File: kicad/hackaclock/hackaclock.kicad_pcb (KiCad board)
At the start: 2 copper layers, 95 x 65 mm, 13 parts, among them J1 Conn_01x08_Pin, SW1 SW_Push, SW2 SW_Push, SW3 SW_Push, SW4 SW_Push, SW5 SW_Push, SW6 SW_Push, U1 XIAO-ESP32-C3-SMD

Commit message: Added stardance logo to silkscreen
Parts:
- added G***: LOGO, LOGO, F.Cu at (41.0, 28.0)

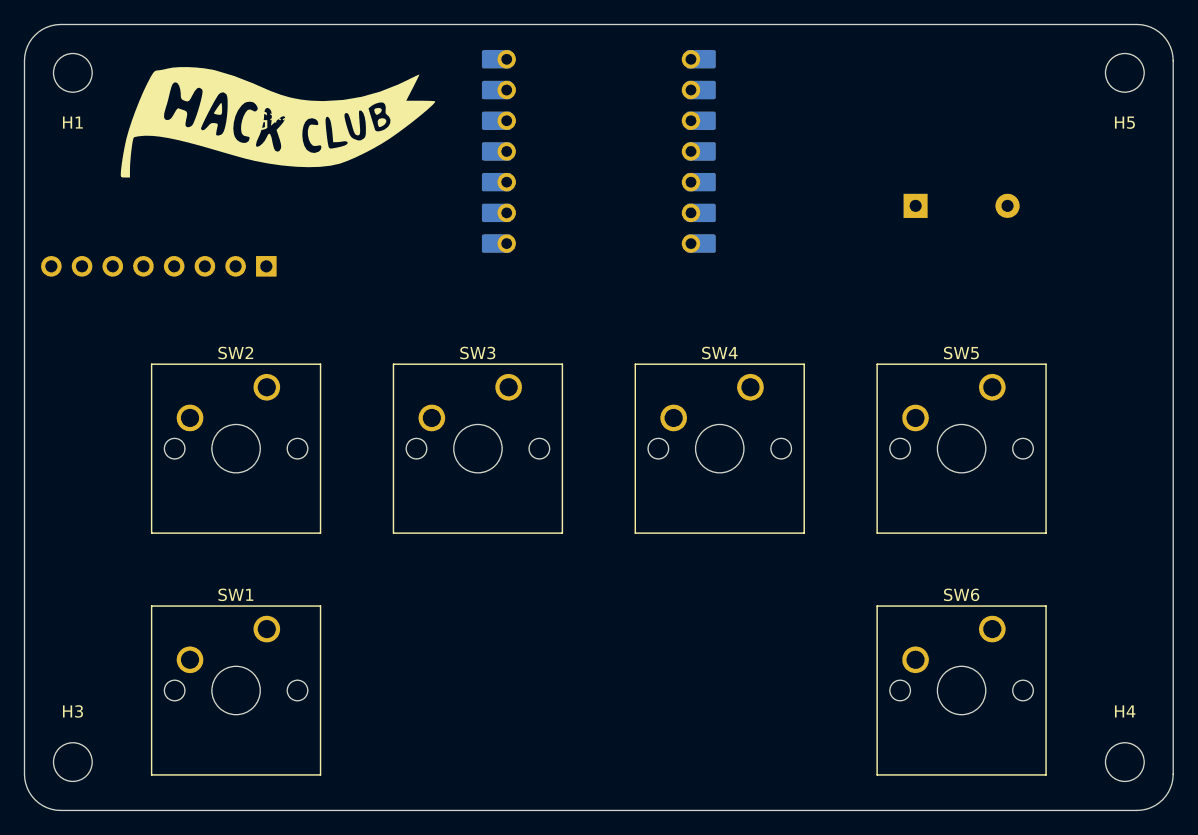
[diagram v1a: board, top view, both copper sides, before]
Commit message: Add traces
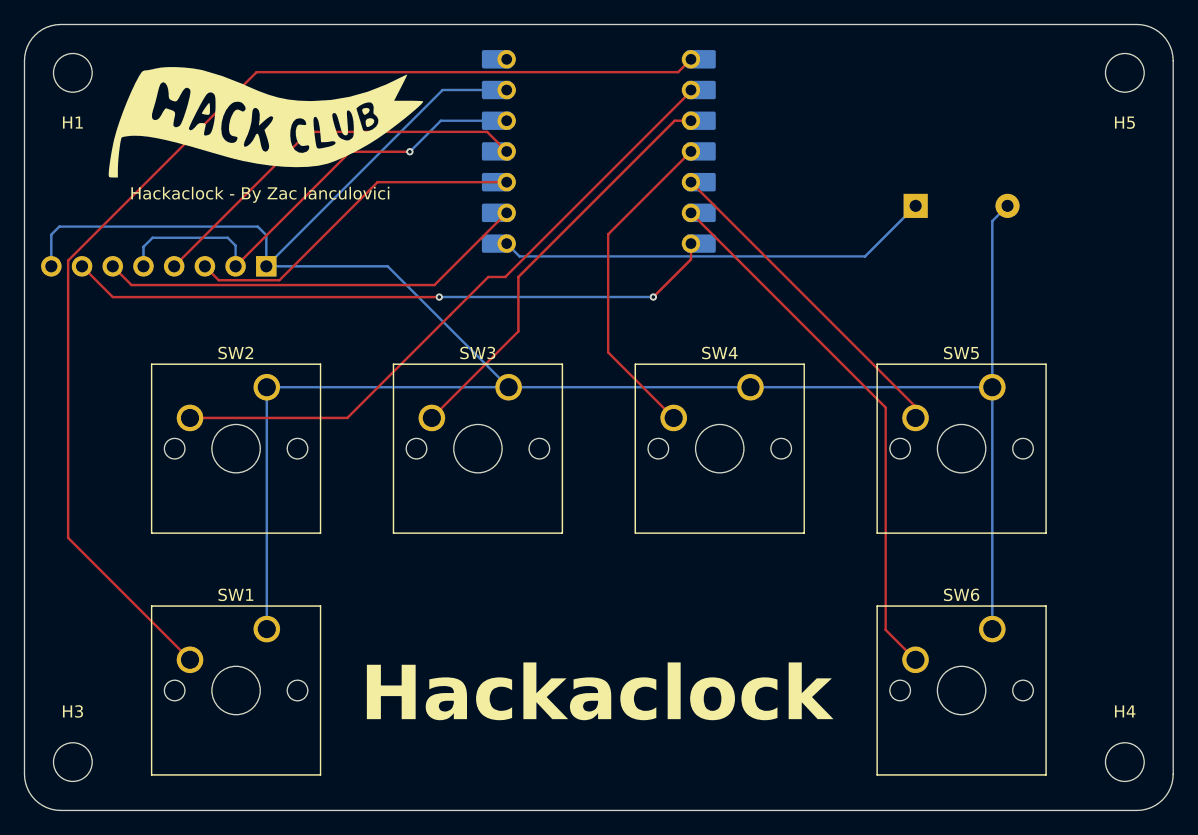
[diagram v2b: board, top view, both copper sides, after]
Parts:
- added Hackaclock - By Zac Ianculovici: LOGO, LOGO, B.Cu at (40.0, 28.0)
- Hackaclock - By Zac Ianculovici: renamed from G***
- moved Hackaclock - By Zac Ianculovici 1.00 mm to (40.0, 28.0)
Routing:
- net GND: track 0.00 -> 188.3 mm
- net Net-(U1-D0): track 0.00 -> 95.6 mm
- net /CS: track 0.00 -> 54.0 mm, vias 0 -> 2
- net Net-(U1-D1): track 0.00 -> 52.7 mm
- net Net-(U1-D5): track 0.00 -> 44.7 mm
- net +3V3: track 0.00 -> 38.1 mm, vias 0 -> 1
- net Net-(BZ1-+): track 0.00 -> 36.0 mm
- net /DC: track 0.00 -> 35.7 mm
- net Net-(U1-D2): track 0.00 -> 34.2 mm
- net /SDA: track 0.00 -> 32.8 mm
- net /SCL: track 0.00 -> 28.8 mm
- net Net-(U1-D4): track 0.00 -> 27.2 mm
- net Net-(U1-D3): track 0.00 -> 27.1 mm
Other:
- board text added: "Hackaclock"
